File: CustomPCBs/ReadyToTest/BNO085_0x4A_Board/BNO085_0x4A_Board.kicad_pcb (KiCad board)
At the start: 4 copper layers, 8.1 x 8.8 mm, 12 parts, among them J1 Conn_01x04_Pin, Y1 32.768kHz

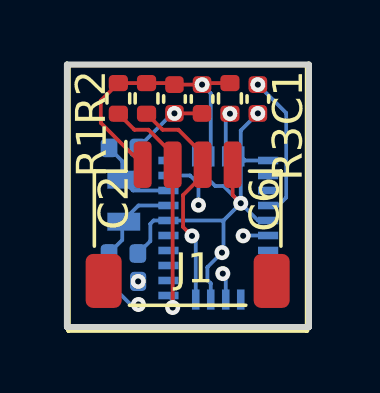
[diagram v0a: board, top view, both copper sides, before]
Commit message: Updating components' 3d models for 3d print cases
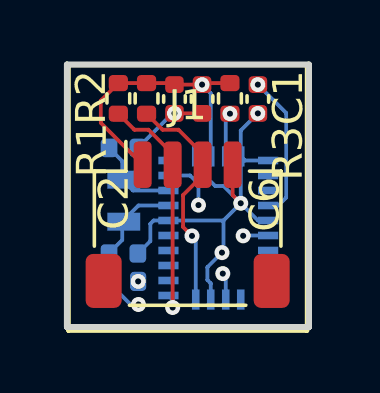
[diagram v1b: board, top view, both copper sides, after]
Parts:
- J1: footprint Connector_JST:JST_SH_SM04B-SRSS-TB_1x04-1MP_P1.00mm_Horizontal -> my_connectors:JST_SH_SM04B-SRSS-TB_1x04-1MP_P1.00mm_Horizontal
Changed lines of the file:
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@@
     )
   )
-  (footprint "Connector_JST:JST_SH_SM04B-SRSS-TB_1x04-1MP_P1.00mm_Horizontal" (layer "F.Cu")
+  (footprint "my_connectors:JST_SH_SM04B-SRSS-TB_1x04-1MP_P1.00mm_Horizontal" (layer "F.Cu")
     (at 98.27 110.36)
     (descr "JST SH series connector, SM04B-SRSS-TB (http://www.jst-mfg.com/product/pdf/eng/eSH.pdf), generated with kicad-footprint-generator")
@@
     (property "ki_keywords" "connector")
     (attr smd)
-    (fp_text reference "J1" (at 0.21 1.46) (layer "F.SilkS")
+    (fp_text reference "J1" (at 0 -3.98) (layer "F.SilkS")
         (effects (font (size 1 1) (thickness 0.15)))
     )
@@
     (pad "4" smd roundrect (at 1.5 -2) (size 0.6 1.55) (layers "F.Cu" "F.Paste" "F.Mask") (roundrect_rratio 0.25)
       (net 12 "GND") (pinfunction "Pin_4") (pintype "passive"))
-    (pad "MP" smd roundrect (at -2.8 1.875) (size 1.2 1.8) (layers "F.Cu" "F.Paste" "F.Mask") (roundrect_rratio 0.2083333333))
-    (pad "MP" smd roundrect (at 2.8 1.875) (size 1.2 1.8) (layers "F.Cu" "F.Paste" "F.Mask") (roundrect_rratio 0.2083333333))
-    (model "${KICAD6_3DMODEL_DIR}/Connector_JST.3dshapes/JST_SH_SM04B-SRSS-TB_1x04-1MP_P1.00mm_Horizontal.wrl"
-      (offset (xyz 0 0 0))
+    (pad "MP" smd roundrect (at -2.8 1.875) (size 1.2 1.8) (layers "F.Cu" "F.Paste" "F.Mask") (roundrect_rratio 0.208333))
+    (pad "MP" smd roundrect (at 2.8 1.875) (size 1.2 1.8) (layers "F.Cu" "F.Paste" "F.Mask") (roundrect_rratio 0.208333))
+    (model "C:/Users/Ruben/Desktop/repositories/KiCADlibraries/my_connectors.pretty/PRT-14417--3DModel-STEP-1.STEP"
+      (offset (xyz 0 1.35 -0.35))
       (scale (xyz 1 1 1))
-      (rotate (xyz 0 0 0))
+      (rotate (xyz -90 0 0))
     )
   )

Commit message: Updating IMU boards for different wire connections
Now all components are placed on one layer, making assembly easier. The
JST connector was dropped for smalled IMU housing, instead the wires now
solder directly to the board and exit from the sides of the board.
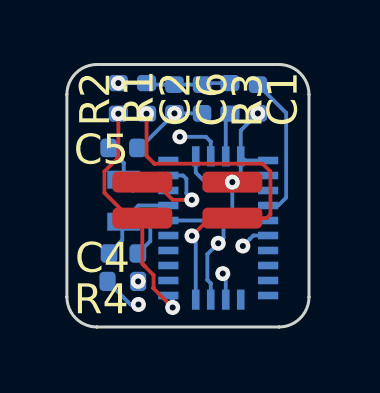
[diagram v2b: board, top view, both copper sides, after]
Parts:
- C1, C2, C6, R1, R2, R3: moved to B.Cu
- J1: footprint my_connectors:JST_SH_SM04B-SRSS-TB_1x04-1MP_P1.00mm_Horizontal -> Library:WireToBoard2x2Wide
- moved J1 0.82 mm to (98.3, 109.5)
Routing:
- net SCL: track 7.73 -> 12.4 mm, vias 1 -> 2
- net +3V3: track 12.6 -> 9.60 mm, vias 4 -> 5
- net GND: track 19.1 -> 17.5 mm
- net SDA: track 7.94 -> 8.31 mm, vias 1 -> 2
- net Net-(U1-CAP): vias 1 -> 0
- net Net-(U1-BOOTN): vias 1 -> 0
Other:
- outline, holes or cut-outs redrawn
